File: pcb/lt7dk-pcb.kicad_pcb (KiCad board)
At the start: 2 copper layers, 62 x 84 mm, 87 parts, among them J1 PINHD_1x8_Male, J2 Conn_01x02, J3 PINHD_1x2_Male, J4 PINHD_1x2_Male, J5 PINHD_1x2_Male, J6 PINHD_1x2_Male, SW1 SW_Push, SW2 SW_Push, SW3 SW_Push, SW4 SW_Push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

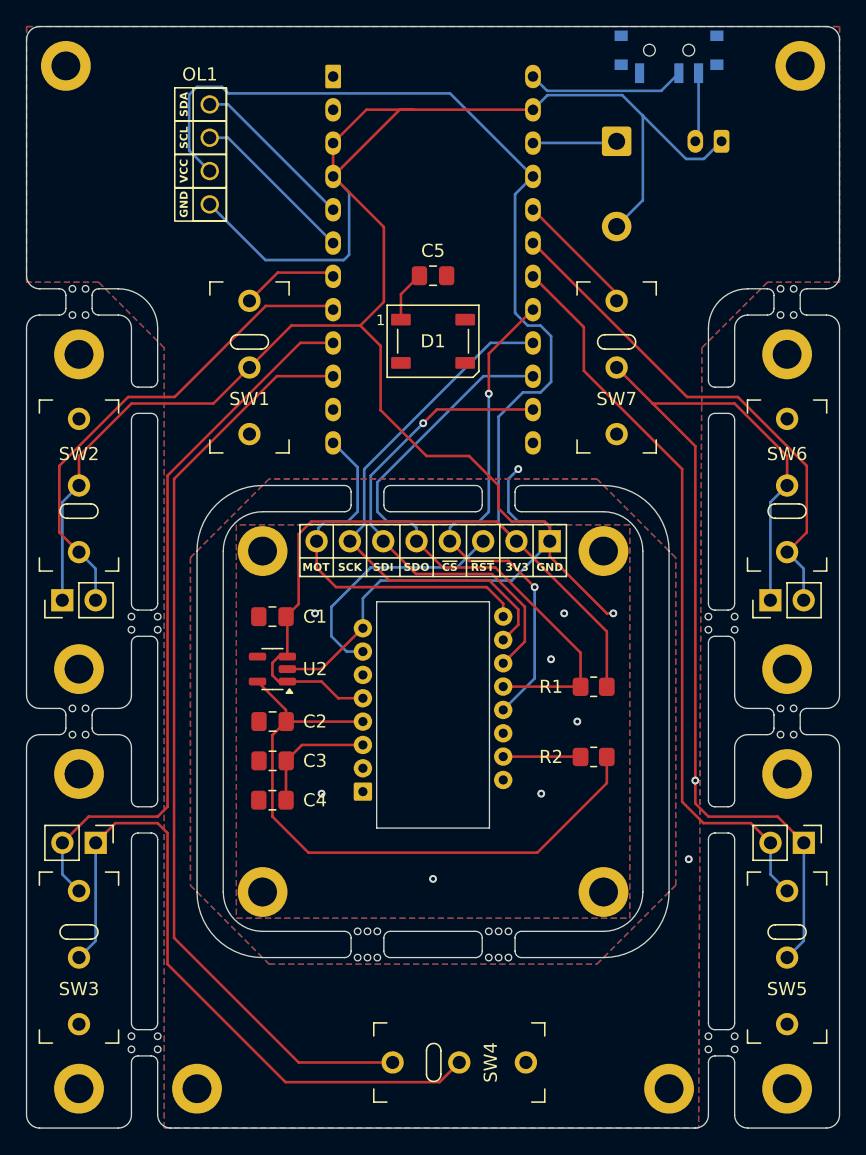
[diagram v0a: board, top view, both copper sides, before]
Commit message: Update mouse bites & add some silkscreen info
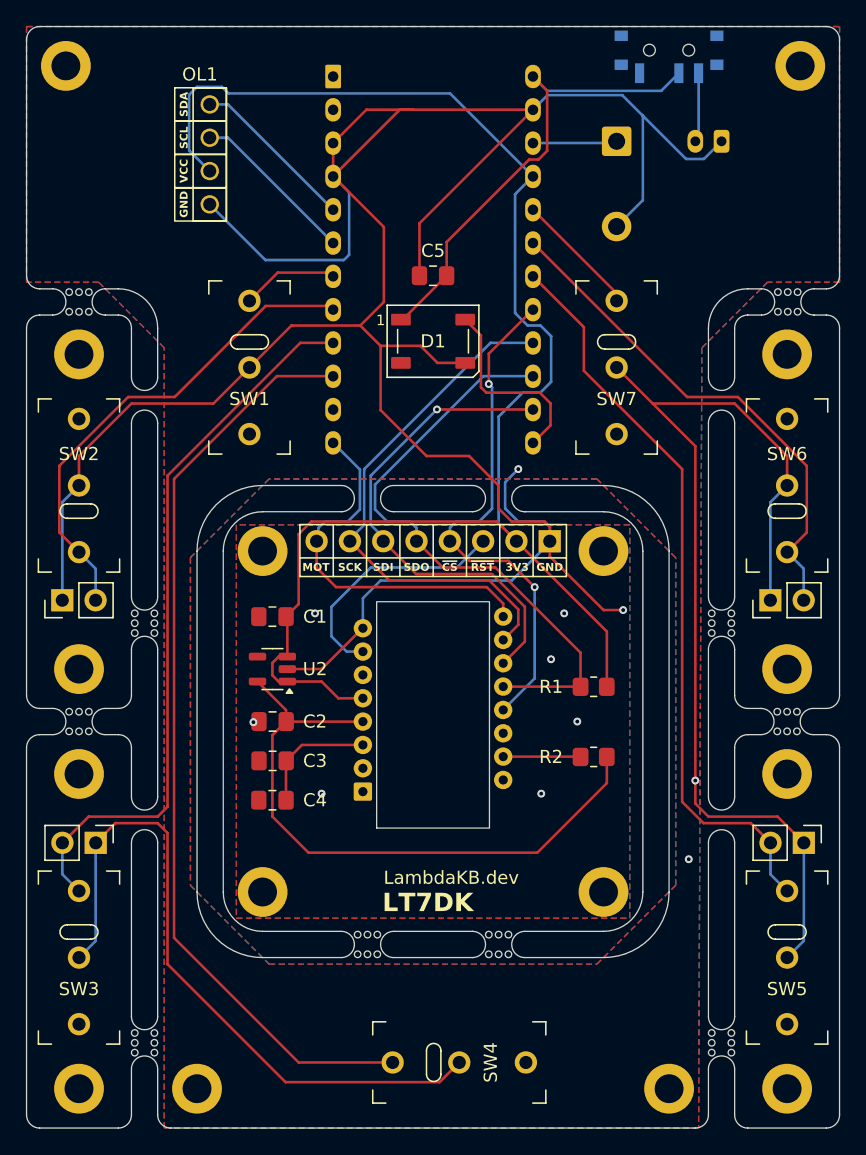
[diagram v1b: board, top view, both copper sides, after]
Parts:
- removed REF** (x44): MoutingHole_0.5mm_NPTH, MountingHole:MoutingHole_0.5mm_NPTH
- added MouseBite_2mm_Slot: VAL**, MouseBite:MouseBite_2mm_Slot, F.Cu at (49.0, 85.5)
- added MouseBite_2mm_Slot: VAL**, MouseBite:MouseBite_2mm_Slot, F.Cu at (93.0, 85.5)
- added MouseBite_2mm_Slot: VAL**, MouseBite:MouseBite_2mm_Slot, F.Cu at (49.0, 117.5)
- added MouseBite_2mm_Slot: VAL**, MouseBite:MouseBite_2mm_Slot, F.Cu at (44.0, 61.0)
- added MouseBite_2mm_Slot: VAL**, MouseBite:MouseBite_2mm_Slot, F.Cu at (98.0, 61.0)
- added MouseBite_2mm_Slot: VAL**, MouseBite:MouseBite_2mm_Slot, F.Cu at (93.0, 117.5)
- added MouseBite_2mm_Slot: VAL**, MouseBite:MouseBite_2mm_Slot, F.Cu at (76.0, 110.0)
- added MouseBite_2mm_Slot: VAL**, MouseBite:MouseBite_2mm_Slot, F.Cu at (66.0, 110.0)
- added MouseBite_2mm_Slot: VAL**, MouseBite:MouseBite_2mm_Slot, F.Cu at (44.0, 93.0)
- added MouseBite_2mm_Slot: VAL**, MouseBite:MouseBite_2mm_Slot, F.Cu at (98.0, 93.0)
- turned C5 to 0 degrees
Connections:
- C5 pad 2: +5V -> /RAW
- D1 pad 1: +5V -> /RAW
- U1 pad 13: unconnected-(U1-D10-Pad13) -> /LED
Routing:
- net /RAW: track 12.2 -> 36.3 mm
- net GND: track 321.9 -> 345.9 mm
- net /LED: track 0.00 -> 15.0 mm
- net +5V: track 3.94 -> 0.00 mm
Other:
- outline, holes or cut-outs redrawn
- board text added: "2025 - LambdaKB.dev"
- board text added: "CERN-OHL-S-2.0"
- board text added: "Documentation: lambdakb.dev/devices/lt7dk/"
- board text added: "LT7DK"
- board text added: "LT7DK v1.00"
- board text added: "LambdaKB.dev"
- board text added: "Licensed under"
- board text added: "PMW3360DM"

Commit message: Update front silkscreen & fix export
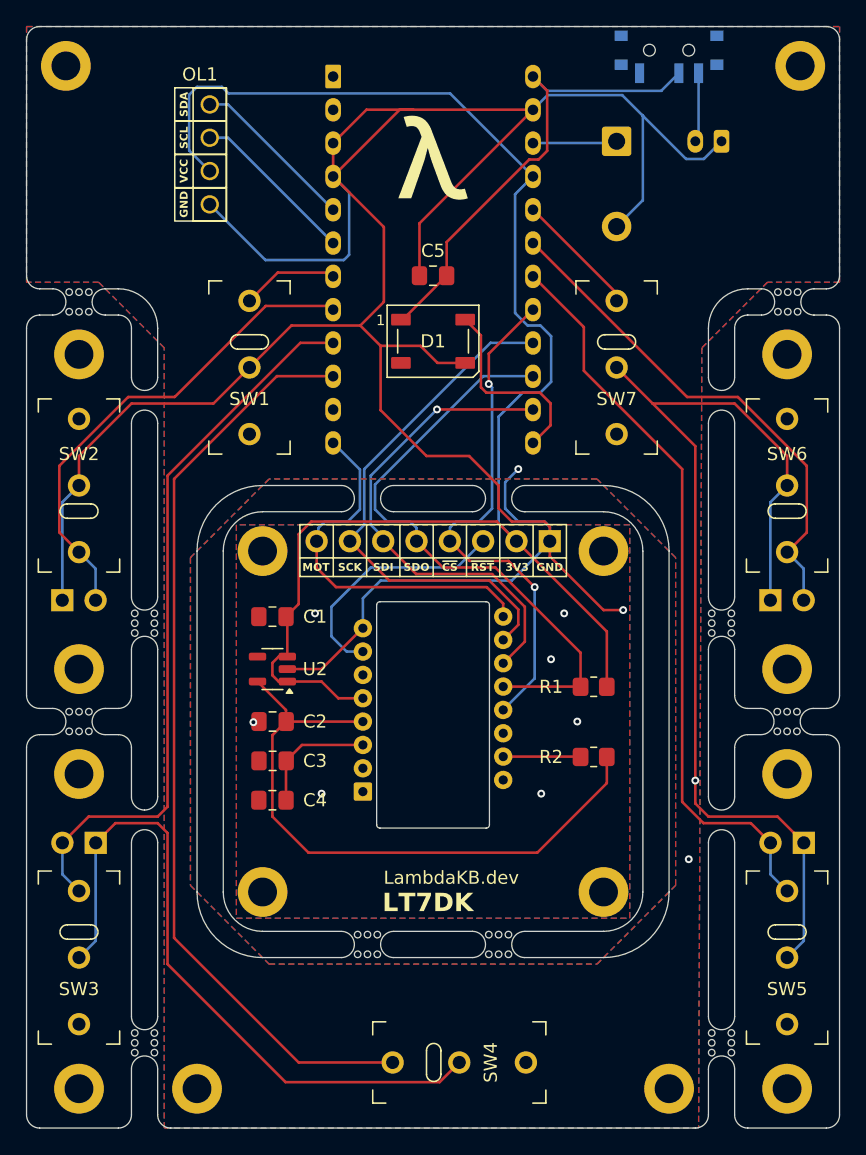
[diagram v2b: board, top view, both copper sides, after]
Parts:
- J3, J4, J5, J6: moved to B.Cu
- turned J3 to -90 degrees
- turned J4 to 90 degrees
- turned J5 to 90 degrees
- turned J6 to -90 degrees
- turned MouseBite_2mm_Slot to -90 degrees
- turned MouseBite_2mm_Slot to 0 degrees
- turned MouseBite_2mm_Slot to 180 degrees
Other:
- outline, holes or cut-outs redrawn

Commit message: Cleanup schematic and pcb
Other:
- board text added: "0.0000 mm / 0.0000 mm"
- board text added: "62.0000 mm x 84.0000 mm"
- board text removed: "0.1270 mm / 0.1270 mm"
- board text removed: "62.0000 mm x 82.0000 mm"
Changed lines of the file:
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@@
 	(paper "A4")
 	(title_block
-		(title "PWM3360 Trackball Kit")
-		(date "2024-12-09")
-		(rev "1")
-		(company "UserCTL.xyz")
+		(title "LT7DK")
+		(date "2025-02-04")
+		(rev "v1.00")
+		(company "LambdaKB.dev")
+		(comment 1 "https://lambdakb.dev/devices/lt7dk/")
 	)
 	(layers
@@
 		(at 98 93 180)
 		(property "Reference" "MouseBite_2mm_Slot"
-			(at 0 -2 360)
+			(at 0 -2 0)
 			(layer "F.SilkS")
 			(hide yes)
@@
 		)
 		(property "Value" "VAL**"
-			(at 0 2.1 360)
+			(at 0 2.1 0)
 			(layer "F.SilkS")
 			(hide yes)
@@
 		)
 		(property "Footprint" "MouseBite:MouseBite_2mm_Slot"
-			(at 0 0 360)
+			(at 0 0 0)
 			(layer "F.Fab")
 			(hide yes)
@@
 		)
 		(property "Datasheet" ""
-			(at 0 0 360)
+			(at 0 0 0)
 			(layer "F.Fab")
 			(hide yes)
@@
 		)
 		(property "Description" ""
-			(at 0 0 360)
+			(at 0 0 0)
 			(layer "F.Fab")
 			(hide yes)
@@
 		(at 66 110)
 		(property "Reference" "MouseBite_2mm_Slot"
-			(at 0 -2 360)
+			(at 0 -2 0)
 			(layer "F.SilkS")
 			(hide yes)
@@
 		)
 		(property "Value" "VAL**"
-			(at 0 2.1 360)
+			(at 0 2.1 0)
 			(layer "F.SilkS")
 			(hide yes)
@@
 		)
 		(property "Footprint" "MouseBite:MouseBite_2mm_Slot"
-			(at 0 0 360)
+			(at 0 0 0)
 			(layer "F.Fab")
 			(hide yes)
@@
 		)
 		(property "Datasheet" ""
-			(at 0 0 360)
+			(at 0 0 0)
 			(layer "F.Fab")
 			(hide yes)
@@
 		)
 		(property "Description" ""
-			(at 0 0 360)
+			(at 0 0 0)
 			(layer "F.Fab")
 			(hide yes)
@@
 		)
 		(fp_text user "${REFERENCE}"
-			(at 0 -1.27 360)
+			(at 0 -1.27 0)
 			(layer "B.Fab")
 			(effects
@@
 		)
 		(fp_text user "${REFERENCE}"
-			(at 0 -1.27 360)
+			(at 0 -1.27 0)
 			(layer "B.Fab")
 			(effects
@@
 		)
 		(fp_text user "${REFERENCE}"
-			(at 0 -1.27 360)
+			(at 0 -1.27 0)
 			(layer "B.Fab")
 			(effects
@@
 		)
 		(fp_text user "${REFERENCE}"
-			(at 0 -1.27 360)
+			(at 0 -1.27 0)
 			(layer "B.Fab")
 			(effects
@@
 		)
 	)
-	(gr_text "Board overall dimensions: "
-		(at 14 178.629 0)
+	(gr_text "2"
+		(at 46.657143 174.744 0)
 		(layer "F.Fab")
 		(effects
@@
 		)
 	)
-	(gr_text "Castellated pads: "
-		(at 14 190.5 0)
+	(gr_text "BOARD CHARACTERISTICS"
+		(at 13.25 169.25 0)
 		(layer "F.Fab")
 		(effects
 			(font
-				(size 1.5 1.5)
-				(thickness 0.2)
+				(size 2 2)
+				(thickness 0.4)
 			)
 			(justify left top)
 		)
 	)
-	(gr_text "Min track/spacing: "
-		(at 14 182.586 0)
+	(gr_text "Edge card connectors: "
+		(at 14 194.529 0)
 		(layer "F.Fab")
 		(effects
@@
 		)
 	)
-	(gr_text "Min hole diameter: "
-		(at 80.814281 182.586 0)
+	(gr_text ""
+		(at 80.814281 178.701 0)
 		(layer "F.Fab")
 		(effects
@@
 		)
 	)
-	(gr_text "No"
-		(at 46.657143 194.457 0)
+	(gr_text "1.6000 mm"
+		(at 105.757138 174.744 0)
 		(layer "F.Fab")
 		(effects
@@
 		)
 	)
-	(gr_text "0.3000 mm"
-		(at 105.757138 182.586 0)
+	(gr_text "Copper Layer Count: "
+		(at 14 174.744 0)
 		(layer "F.Fab")
 		(effects
@@
 		)
 	)
-	(gr_text "No"
-		(at 105.757138 186.543 0)
+	(gr_text "0.3000 mm"
+		(at 105.757138 182.658 0)
 		(layer "F.Fab")
 		(effects
@@
 		)
 	)
-	(gr_text "No"
-		(at 105.757138 190.5 0)
+	(gr_text "0.0000 mm / 0.0000 mm"
+		(at 46.657143 182.658 0)
 		(layer "F.Fab")
 		(effects
@@
 		)
 	)
-	(gr_text "HAL lead-free"
-		(at 46.657143 186.543 0)
+	(gr_text "Castellated pads: "
+		(at 14 190.572 0)
 		(layer "F.Fab")
 		(effects
@@
 	)
 	(gr_text ""
-		(at 80.814281 178.629 0)
+		(at 105.757138 178.701 0)
 		(layer "F.Fab")
 		(effects
@@
 		)
 	)
-	(gr_text "Edge card connectors: "
-		(at 14 194.457 0)
+	(gr_text "Board Thickness: "
+		(at 80.814281 174.744 0)
 		(layer "F.Fab")
 		(effects
@@
 		)
 	)
-	(gr_text "BOARD CHARACTERISTICS"
-		(at 13.25 169.178 0)
+	(gr_text "Copper Finish: "
+		(at 14 186.615 0)
 		(layer "F.Fab")
 		(effects
 			(font
-				(size 2 2)
-				(thickness 0.4)
+				(size 1.5 1.5)
+				(thickness 0.2)
 			)
 			(justify left top)
 		)
 	)
-	(gr_text ""
-		(at 105.757138 178.629 0)
+	(gr_text "62.0000 mm x 84.0000 mm"
+		(at 46.657143 178.701 0)
 		(layer "F.Fab")
 		(effects
@@
 		)
 	)
-	(gr_text "0.1270 mm / 0.1270 mm"
-		(at 46.657143 182.586 0)
+	(gr_text "No"
+		(at 46.657143 190.572 0)
 		(layer "F.Fab")
 		(effects
@@
 		)
 	)
-	(gr_text "Copper Finish: "
-		(at 14 186.543 0)
+	(gr_text "Plated Board Edge: "
+		(at 80.814281 190.572 0)
 		(layer "F.Fab")
 		(effects
@@
 		)
 	)
-	(gr_text "Board Thickness: "
-		(at 80.814281 174.672 0)
+	(gr_text "HAL lead-free"
+		(at 46.657143 186.615 0)
 		(layer "F.Fab")
 		(effects
@@
 		)
 	)
-	(gr_text "Impedance Control: "
-		(at 80.814281 186.543 0)
+	(gr_text "Min track/spacing: "
+		(at 14 182.658 0)
 		(layer "F.Fab")
 		(effects
@@
 		)
 	)
-	(gr_text "1.6000 mm"
-		(at 105.757138 174.672 0)
+	(gr_text "No"
+		(at 46.657143 194.529 0)
 		(layer "F.Fab")
 		(effects
@@
 		)
 	)
-	(gr_text "62.0000 mm x 82.0000 mm"
-		(at 46.657143 178.629 0)
+	(gr_text "No"
+		(at 105.757138 186.615 0)
 		(layer "F.Fab")
 		(effects
@@
 		)
 	)
-	(gr_text "Copper Layer Count: "
-		(at 14 174.672 0)
+	(gr_text "Board overall dimensions: "
+		(at 14 178.701 0)
 		(layer "F.Fab")
 		(effects
@@
 		)
 	)
-	(gr_text "Plated Board Edge: "
-		(at 80.814281 190.5 0)
+	(gr_text "Min hole diameter: "
+		(at 80.814281 182.658 0)
 		(layer "F.Fab")
 		(effects
@@
 		)
 	)
-	(gr_text "2"
-		(at 46.657143 174.672 0)
+	(gr_text "Impedance Control: "
+		(at 80.814281 186.615 0)
 		(layer "F.Fab")
 		(effects
@@
 	)
 	(gr_text "No"
-		(at 46.657143 190.5 0)
+		(at 105.757138 190.572 0)
 		(layer "F.Fab")
 		(effects
@@
 	)
 	(group "group-boardCharacteristics"
-		(members "00397072-5d0f-417e-84e7-04de6aec060f" "03a6c7d4-2bae-4bc1-8927-ce3448f09fd6"
-			"1e50947c-9fc7-4223-9cd9-1231ee5a872a" "2af2b2e2-a44a-485b-85ab-3a75be3cd4ee"
-			"306679fc-a7d1-4b52-bcff-bef4b3b4d2f1" "4261aece-f2f8-4586-bf9e-571d2e34b5d4"
-			"4d5620d1-2bdc-4fb9-8627-8c0d25fed9a3" "58413ed2-91df-42bb-9fc8-548d0bef5cac"
-			"58a8a338-774d-48d0-90c7-bf79a79d2ec1" "6831b7e5-b2cc-46a9-a04f-6655beaba4cb"
-			"68ca08d9-d68a-400c-a4be-a56aab669cb2" "69e607d2-e597-4515-8a73-5153b7846baf"
-			"72ab29cd-a4e6-44f4-8765-b335dca5932b" "79a0b2fe-266e-4438-9f16-056fb3702b66"
-			"7e188eef-6ce9-4c83-9138-f6bd2c758aee" "8558df77-2e83-4dcd-8055-895f3721b50e"
-			"9b0ca205-9fff-4ac2-8773-cb6a571cb70f" "9f1a18f9-2566-4bc6-bf0b-fc6a02390122"
-			"bb402f57-22a8-4146-b033-ee01da6296a7" "ecfa7fcb-a9f6-46d6-8d48-2f1da82f5d78"
-			"efb5a0ca-99d8-4e7a-a8c6-cd0214f4faa3" "f27776c0-0e8c-4dfc-9e21-9da194e0b0d3"
-			"f40067ba-60d4-4734-b98d-cc867baeca9b"
+		(members "0990cac2-5b07-4c3e-8cda-1c235d1bf820" "0a7b590c-467e-4ab0-8be2-f06c012ef71f"
+			"14a5e281-5aec-4e5c-b606-5662357b3e0a" "29cbd3ce-7a7a-4d34-953e-92d30487f759"
+			"37637103-a00a-46ed-adc6-22c83c44a26c" "469b92eb-cd9e-4f29-9491-3e9beba45f6c"
+			"49b242d6-a2a0-4617-87f4-12abff7b5696" "4ed5844a-467c-4554-90c3-211a5b7e9b40"
+			"562034f4-c8f8-471a-aa95-218e8d163128" "6e2e64ec-4aaa-49c2-bf97-94cd9d1c4261"
+			"79ab6484-a22f-4840-9ad3-ab01fab413d4" "7bdcbc9c-40b8-4a97-899d-5f8f82ea10b2"
+			"85341b6f-e26c-4d6c-886d-7fa90684affa" "8e0161e7-3a98-42ce-96ce-6af8ec615fdc"
+			"94f71f38-2321-474f-9931-5312b5a0f242" "ad0beb04-d4d9-47b2-a07c-fd3fce8d02e6"
+			"b43ab33e-9dd3-4f98-a6b9-67033356e3de" "c2baaaf1-c3cf-419d-9c75-d7440ebf69b5"
+			"c34895df-7124-4973-8209-e227e50e9a39" "cdaf6818-b9ae-4b33-9865-dd0950bd8fdb"
+			"e39ebaba-6e4c-4810-9e3b-8b8a02d0dab1" "e3f17aa3-f6d3-47b4-b633-95b94579ca36"
+			"ea534039-4ea8-4fb2-867f-94c93a53b664"
 		)
 	)

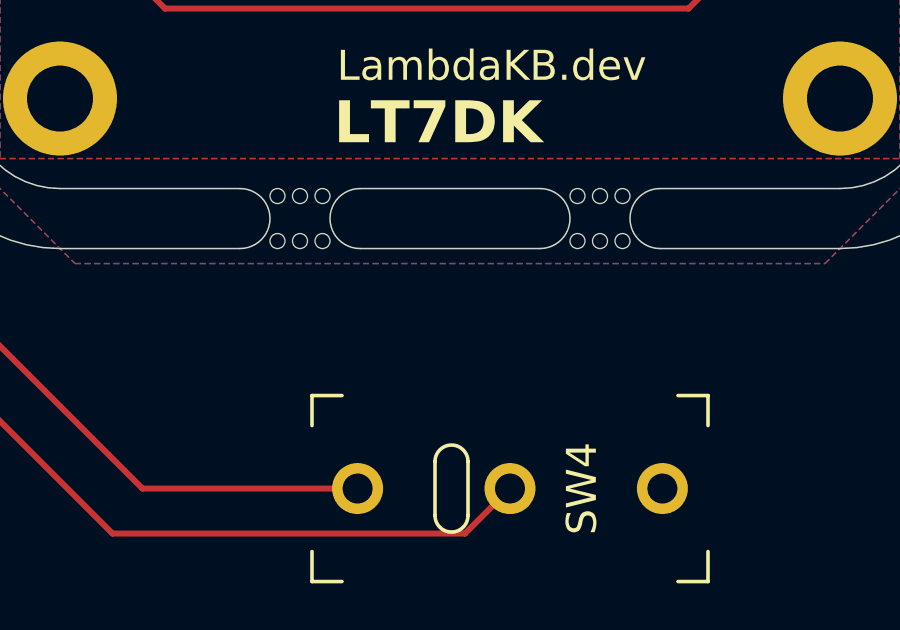
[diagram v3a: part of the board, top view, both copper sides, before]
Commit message: Add more info to back silkscreen
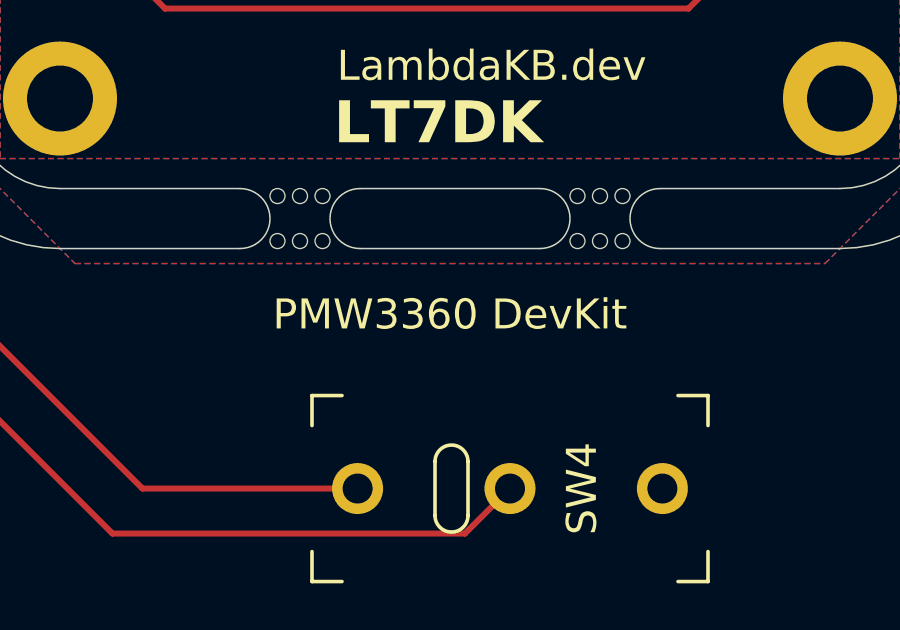
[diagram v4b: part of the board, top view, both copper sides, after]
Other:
- board text added: "(c) 2025 - LambdaKB.dev"
- board text added: "PMW3360 DevKit"
- board text added: "Source: github.com/lambdakb/trackball-lt7dk"
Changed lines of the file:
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@@
+		)
+	)
+	(gr_text "(c) 2025 - LambdaKB.dev"
+		(at 71 122 0)
+		(layer "B.SilkS")
+		(effects
+			(font
+				(size 1 1)
+				(thickness 0.2)
+				(bold yes)
+			)
+			(justify mirror)
 		)
 	)
@@
 		)
 	)
+	(gr_text "Source:\ngithub.com/lambdakb/trackball-lt7dk"
+		(at 71 114 0)
+		(layer "B.SilkS")
+		(effects
+			(font
+				(size 0.8 0.8)
+				(thickness 0.15)
+			)
+			(justify mirror)
+		)
+	)
 	(gr_text "SCK"
 		(at 64.6604 81.2312 0)
@@
 		)
 	)
+	(gr_text "PMW3360 DevKit"
+		(at 71 71.4 0)
+		(layer "B.SilkS")
+		(effects
+			(font
+				(size 0.8 0.8)
+				(thickness 0.15)
+				(bold yes)
+			)
+			(justify mirror)
+		)
+	)
 	(gr_text "SDI"
 		(at 67.2004 81.2312 0)
@@
 				(size 0.6 0.6)
 				(thickness 0.12)
+				(bold yes)
+			)
+			(justify mirror)
+		)
+	)
+	(gr_text "LT7DK"
+		(at 71 69.6 0)
+		(layer "B.SilkS")
+		(effects
+			(font
+				(size 1.2 1.2)
+				(thickness 0.24)
 				(bold yes)
 			)
@@
 		)
 	)
+	(gr_text "PMW3360 DevKit"
+		(at 71 113.2 0)
+		(layer "F.SilkS")
+		(effects
+			(font
+				(size 1 1)
+				(thickness 0.15)
+			)
+		)
+	)
